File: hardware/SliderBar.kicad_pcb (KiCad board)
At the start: 2 copper layers, 54.7 x 25.4 mm, 36 parts, among them J1 USB_B_Mini, J2 MOTOR_OUT, J3 POT_IN, J4 DEBUG, U1 MIC5205-3.3YM5, U2 TB6612FNG, U3 MT3608, U4 STM32F072C8Tx

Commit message: Route some more traces
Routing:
- net GND: track 75.2 -> 132.7 mm, vias 0 -> 6
- net POT: track 0.00 -> 35.9 mm
- net +3V3: track 19.6 -> 40.8 mm, vias 0 -> 3
- net MOT_OUT_1: track 10.9 -> 9.51 mm
- net +10V: track 35.7 -> 37.1 mm
- net Net-(D1-Pad2): track 18.7 -> 19.7 mm
- net SWDIO: track 11.2 -> 10.6 mm
- added copper zone on F.Cu, net +3V3
- removed copper zone on F.Cu, net GND

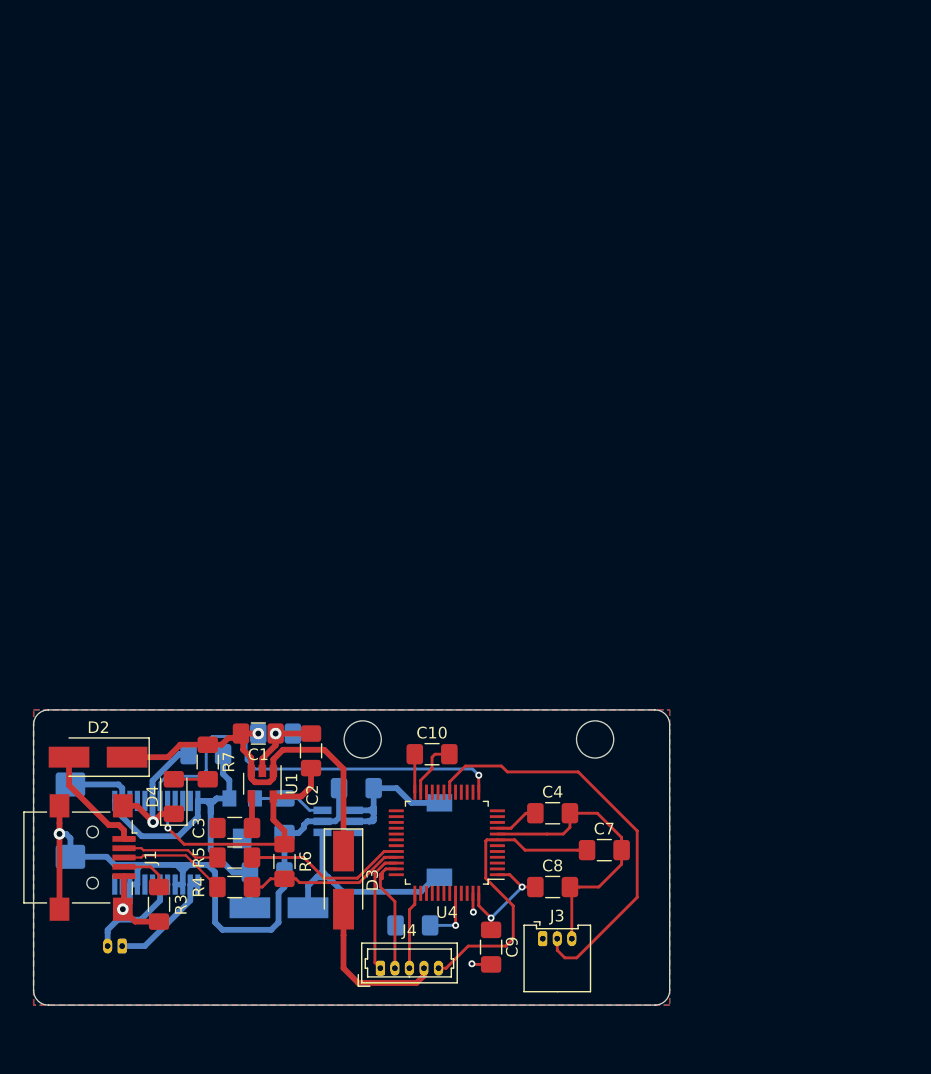
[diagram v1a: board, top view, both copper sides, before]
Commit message: Trying to add LUA to project
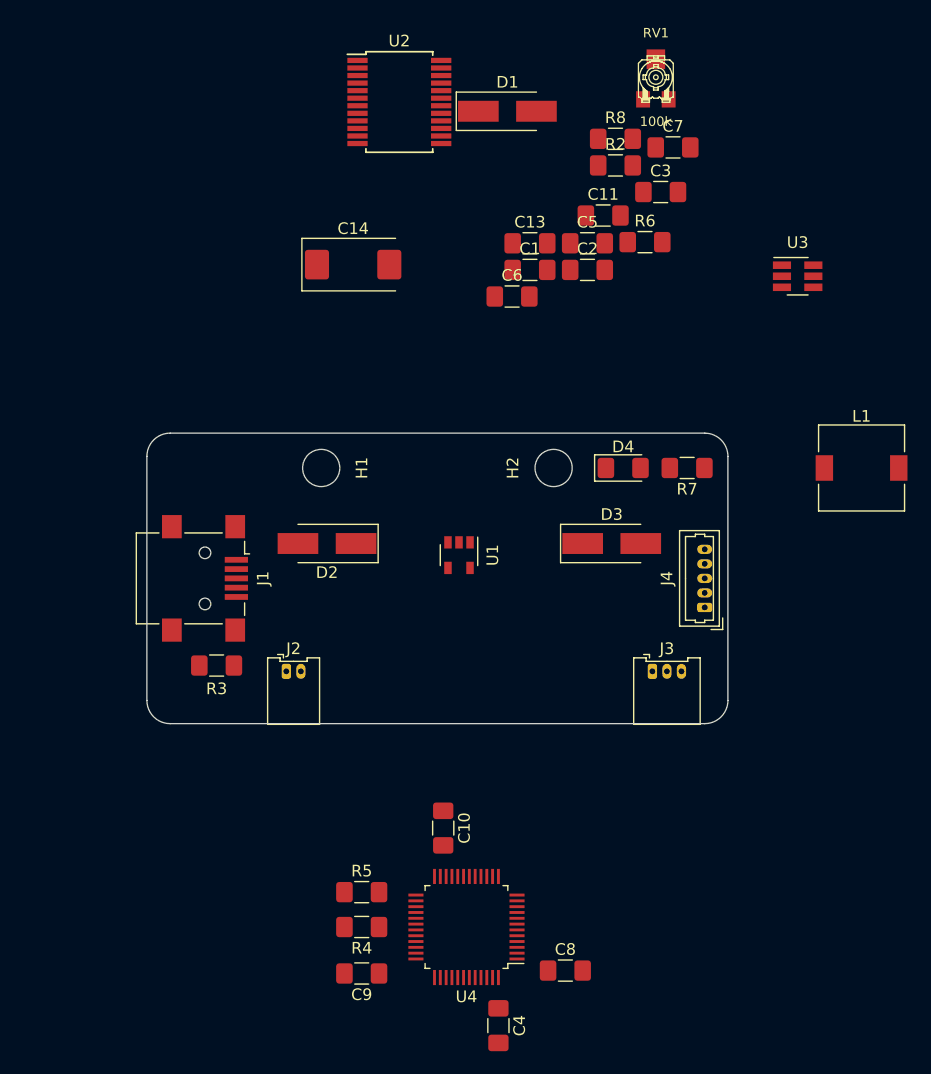
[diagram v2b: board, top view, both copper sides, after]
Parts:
- C11, C13, C14, C5, C6, D1, J2, L1, R2, R8, RV1, U2, U3: moved to F.Cu
- moved RV1 73.2 mm to (148.8, 29.4)
- moved D1 71.3 mm to (136.0, 32.3)
- moved R8 69.9 mm to (145.3, 34.7), turned to 0 degrees
- moved U2 67.1 mm to (126.7, 31.5), turned to 0 degrees
- moved C3 65.9 mm to (149.2, 39.3), turned to 0 degrees
- moved R2 62.8 mm to (145.3, 37.0), turned to 0 degrees
- moved R6 61.7 mm to (147.9, 43.6), turned to 0 degrees
- moved U3 61.3 mm to (161.0, 46.5)
- moved C7 60.8 mm to (150.3, 35.4)
- moved C6 53.8 mm to (136.4, 48.2), turned to 0 degrees
- moved C14 53.7 mm to (122.8, 45.5), turned to 0 degrees
- moved C11 52.7 mm to (144.3, 41.3)
- moved C13 52.1 mm to (138.0, 43.7)
- moved C5 50.9 mm to (142.9, 43.7), turned to 0 degrees
- moved L1 48.4 mm to (166.5, 63.0), turned to 0 degrees
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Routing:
- net GND: track 132.7 -> 0.00 mm, vias 6 -> 0
- net +5V: track 48.2 -> 0.00 mm, vias 1 -> 0
- net +3V3: track 40.8 -> 0.00 mm, vias 3 -> 0
- net +10V: track 37.1 -> 0.00 mm
- net POT: track 35.9 -> 0.00 mm
- net STBY: track 35.8 -> 0.00 mm, vias 1 -> 0
- net NRST: track 26.0 -> 0.00 mm
- net Net-(D1-Pad2): track 19.7 -> 0.00 mm
- net USB_DN: track 14.1 -> 0.00 mm
- net USB_DP: track 13.7 -> 0.00 mm
- net VPP: track 13.4 -> 0.00 mm
- net SWDIO: track 10.6 -> 0.00 mm
- net VBUS: track 10.2 -> 0.00 mm
- net MOT_OUT_1: track 9.51 -> 0.00 mm
- net /D+: track 9.24 -> 0.00 mm
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- removed copper zone on F.Cu, net +3V3
- removed copper zone on B.Cu, net GND
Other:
- board size 54.7 x 25.4 mm -> 50 x 25 mm
- net class Power: clearance 0.15 -> 0.13; trace_width 0.5 -> 0.4; via_dia 1 -> 0.8; via_drill 0.5 -> 0.4
- rule pad_to_mask_clearance: 0.0502 -> 0
